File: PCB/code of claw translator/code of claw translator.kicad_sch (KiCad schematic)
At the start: 43 parts, among them J1 Conn_01x20_Socket, J10 Conn_01x01_Socket, J11 Conn_01x03_Socket, J12 Conn_01x01_Socket, J13 Conn_01x01_Socket, J14 Conn_01x01_Socket, J15 Conn_01x01_Socket, J16 Conn_01x01_Socket, J17 Conn_01x01_Socket, J18 Conn_01x01_Socket, J19 Conn_01x01_Socket, J2 Conn_01x20_Socket, J20 Conn_01x01_Socket, J21 Conn_01x01_Socket, J22 Conn_01x01_Socket, J23 Conn_01x01_Socket, J24 Conn_01x01_Socket, J25 Conn_01x01_Socket, J26 Conn_01x01_Socket, J27 Conn_01x01_Socket, J3 Conn_01x14_Socket, J32 Conn_01x01_Socket, J33 Conn_01x01_Socket, J34 Conn_01x01_Socket, J35 Conn_01x01_Socket, J36 Conn_01x01_Socket, J37 Conn_01x01_Socket, J38 Conn_01x01_Socket, J39 Conn_01x01_Socket, J4 Conn_01x08_Socket, J40 Conn_01x01_Socket, J41 Conn_01x01_Socket, J42 Conn_01x01_Socket, J43 Conn_01x01_Socket, J5 Conn_01x08_Socket, J6 Conn_01x06_Socket, J7 Conn_01x01_Socket, J8 Conn_01x01_Socket, J9 Conn_01x01_Socket

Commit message: Finished rough draft of components in PCB. Now need to wire them up.
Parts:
- removed J34, J35, J38, J39, J42, J43: Conn_01x01_Socket, Connector_PinSocket_2.54mm:PinSocket_1x01_P2.54mm_Horizontal, symbol Connector:Conn_01x01_Socket
- J6: footprint Connector_PinSocket_2.54mm:PinSocket_1x06_P2.54mm_Horizontal -> Connector_PinSocket_2.54mm:PinSocket_1x06_P2.54mm_Vertical
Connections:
- net A10: now also J33.1 (Pin_1)
- net A11: now also J25.1 (Pin_1); no longer J26.1 (Pin_1)
- net A12: now also J17.1 (Pin_1); no longer J18.1 (Pin_1)
- net A8: now also J37.1 (Pin_1)
- net A9: now also J41.1 (Pin_1)
- net B1: now also J13.1 (Pin_1); no longer J14.1 (Pin_1)
- net B13: now also J21.1 (Pin_1); no longer J22.1 (Pin_1)
- no-connect marks 43 -> 37

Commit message: Finished rough PCB routing
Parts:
- J1, J2: now not fitted
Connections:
- no-connect marks 37 -> 23
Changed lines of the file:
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@@
 	)
 	(no_connect
-		(at 215.9 36.83)
-	)
-	(no_connect
 		(at 143.51 93.98)
 	)
@@
 	)
 	(no_connect
-		(at 215.9 72.39)
-	)
-	(no_connect
 		(at 162.56 55.88)
 	)
 	(no_connect
-		(at 195.58 64.77)
-	)
-	(no_connect
 		(at 44.45 20.32)
 	)
 	(no_connect
-		(at 215.9 54.61)
-	)
-	(no_connect
 		(at 143.51 96.52)
 	)
@@
 	)
 	(no_connect
-		(at 195.58 54.61)
-	)
-	(no_connect
-		(at 215.9 41.91)
-	)
-	(no_connect
 		(at 125.73 99.06)
 	)
 	(no_connect
-		(at 215.9 44.45)
-	)
-	(no_connect
-		(at 215.9 57.15)
-	)
-	(no_connect
 		(at 125.73 88.9)
 	)
@@
 	)
 	(no_connect
-		(at 195.58 67.31)
-	)
-	(no_connect
 		(at 143.51 88.9)
 	)
 	(no_connect
-		(at 195.58 52.07)
-	)
-	(no_connect
 		(at 78.74 22.86)
 	)
@@
 	)
 	(no_connect
-		(at 215.9 69.85)
-	)
-	(no_connect
-		(at 215.9 64.77)
-	)
-	(no_connect
 		(at 162.56 53.34)
 	)
@@
 		(at 162.56 50.8)
 	)
-	(no_connect
-		(at 215.9 67.31)
-	)
-	(no_connect
-		(at 215.9 74.93)
-	)
 	(polyline
 		(pts
@@
 		(in_bom yes)
 		(on_board yes)
-		(dnp no)
+		(dnp yes)
 		(property "Reference" "J1"
 			(at 190.5 20.574 0)
@@
 		(in_bom yes)
 		(on_board yes)
-		(dnp no)
+		(dnp yes)
 		(property "Reference" "J2"
 			(at 220.98 20.574 0)

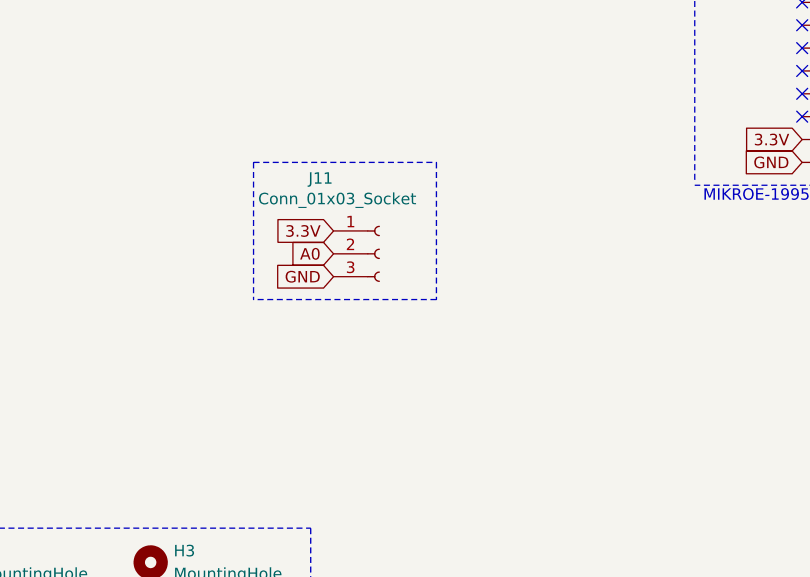
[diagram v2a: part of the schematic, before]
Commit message: Added code for a potentiometer to control sensitivity of the microphone, but might not include it in the final design:
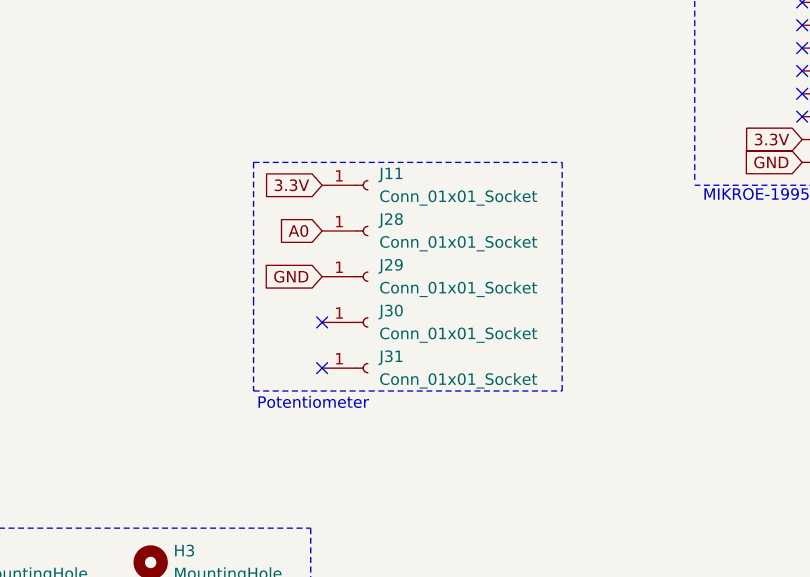
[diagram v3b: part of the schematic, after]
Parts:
- removed J11: Conn_01x03_Socket, Connector_PinSocket_2.54mm:PinSocket_1x03_P2.54mm_Vertical, symbol Connector:Conn_01x03_Socket
- added J11, J28, J29, J30, J31: Conn_01x01_Socket, Connector_PinSocket_2.54mm:PinSocket_1x01_P2.54mm_Vertical, symbol Connector:Conn_01x01_Socket
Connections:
- net 3.3V: now also J11.1 (Pin_1)
- net A0: now also J28.1 (Pin_1)
- net GND: now also J29.1 (Pin_1)
- no-connect marks 23 -> 25
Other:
- note added: "Potentiometer"

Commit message: Ready PCB ready to print
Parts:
- removed J11, J28, J29, J30, J31: Conn_01x01_Socket, Connector_PinSocket_2.54mm:PinSocket_1x01_P2.54mm_Vertical, symbol Connector:Conn_01x01_Socket
- added H5, H6, H7, H8: MountingHole, MountingHole:MountingHole_3.2mm_M3, symbol Mechanical:MountingHole
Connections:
- no-connect marks 25 -> 23
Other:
- note added: "M3"
- note removed: "Potentiometer"

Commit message: Finally finished PCB, submitted it for manufacturing
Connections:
- net 5V: no longer J8.1 (Pin_1)
- new net 5V_S: J8.1 (Pin_1)
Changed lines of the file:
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@@
 		)
 	)
-	(global_label "5V"
+	(global_label "5V_S"
 		(shape input)
 		(at 139.7 143.51 180)
@@
 		)
 		(property "Intersheetrefs" "${INTERSHEET_REFS}"
-			(at 134.4167 143.51 0)
+			(at 132.2396 143.51 0)
 			(effects
 				(font
